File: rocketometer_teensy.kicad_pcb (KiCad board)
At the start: 2 copper layers, 17.8 x 61 mm, 3 parts, among them J101 Teensy4.1, J102 STANDOFF, J103 STANDOFF

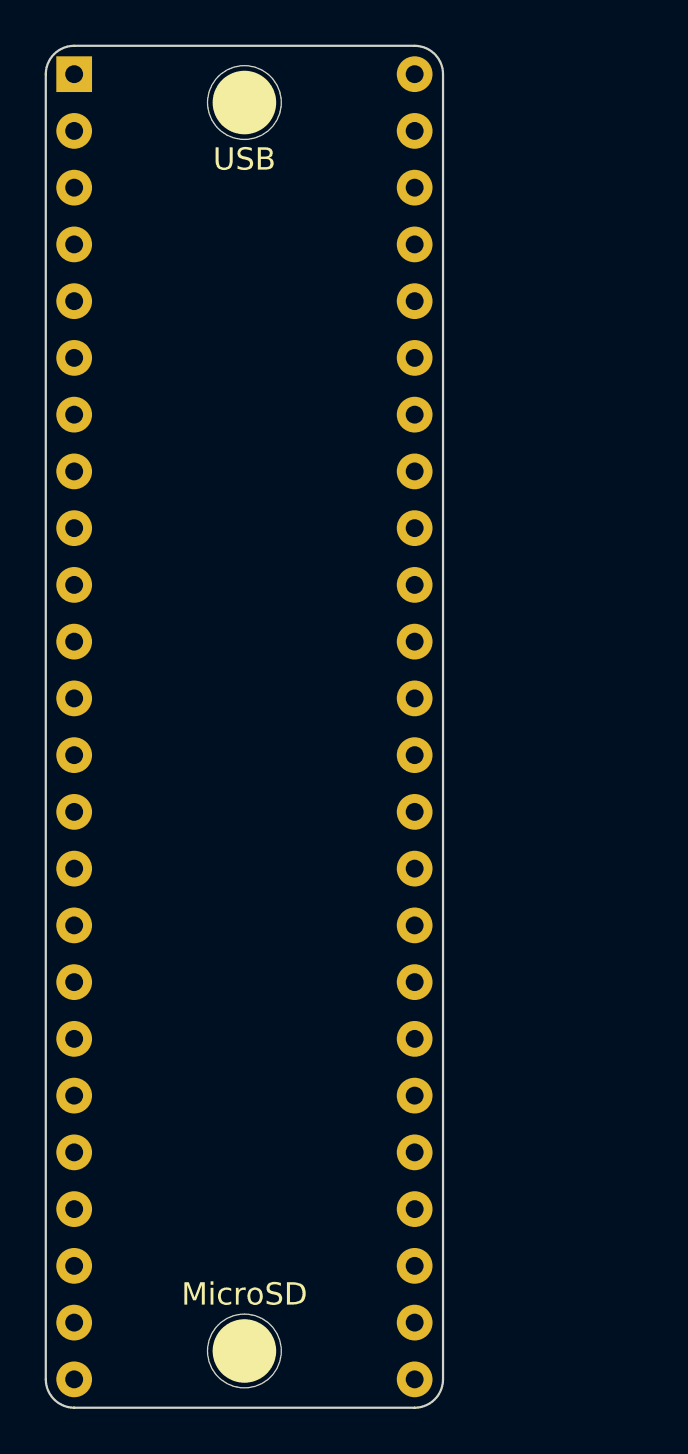
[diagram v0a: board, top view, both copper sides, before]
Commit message: Moved ICM-20948 schematic to kwan_kicad_lib
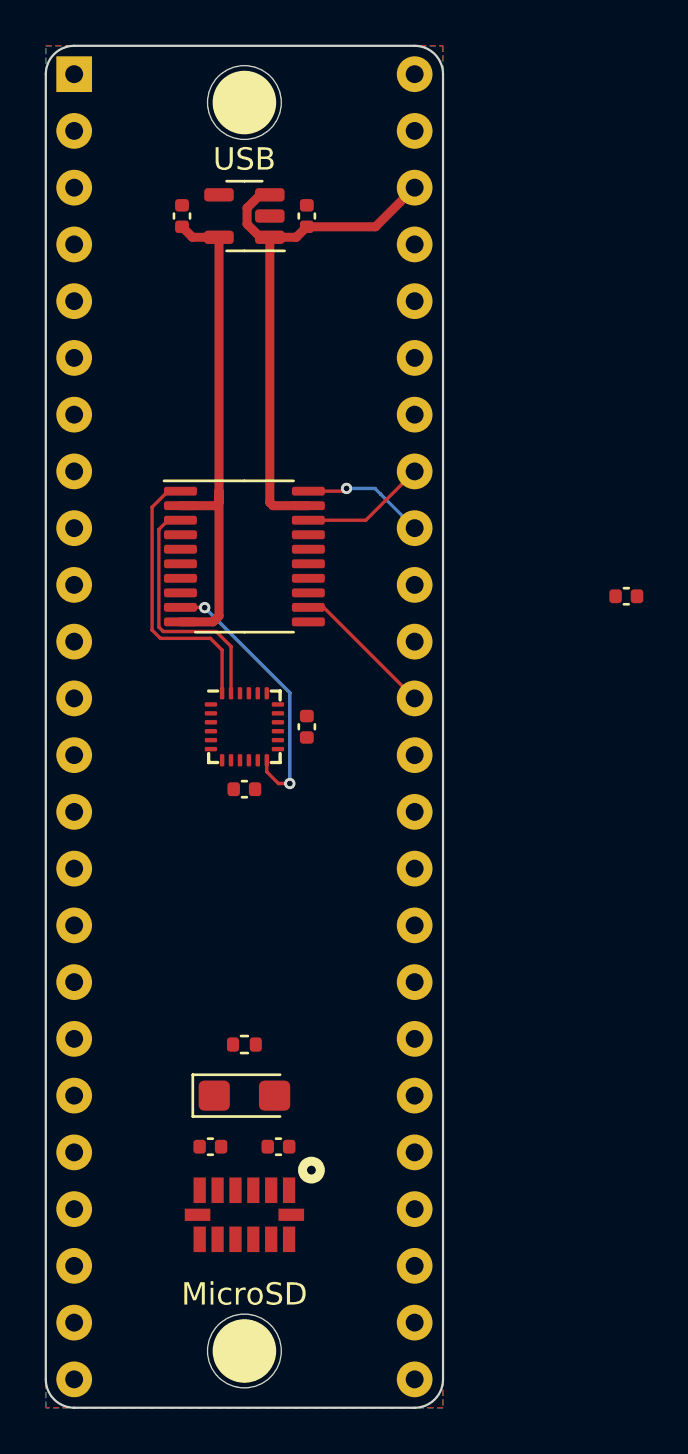
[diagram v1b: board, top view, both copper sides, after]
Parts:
- added C208: 100nF, Capacitor_SMD:C_0402_1005Metric, F.Cu at (138.4, 109.5)
- added C210: 100nF, Capacitor_SMD:C_0402_1005Metric, F.Cu at (155.5, 100.8)
- added C213: 100nF, Capacitor_SMD:C_0402_1005Metric, F.Cu at (141.2, 106.7)
- added C301: 1uF, Capacitor_SMD:C_0402_1005Metric, F.Cu at (141.2, 83.8)
- added C305: 1uF, Capacitor_SMD:C_0402_1005Metric, F.Cu at (135.6, 83.8)
- added C401: 100nF, Capacitor_SMD:C_0402_1005Metric, F.Cu at (140.0, 125.5)
- added C405: 100nF, Capacitor_SMD:C_0402_1005Metric, F.Cu at (136.9, 125.5)
- added C406: 10uF, Capacitor_Tantalum_SMD:CP_EIA-3216-18_Kemet-A, F.Cu at (138.4, 123.2)
- added R406: 100, Resistor_SMD:R_0402_1005Metric, F.Cu at (138.4, 120.9)
- added U101: TXS0108EPW, Package_SO:TSSOP-20_4.4x6.5mm_P0.65mm, F.Cu at (138.4, 99.1)
- added U201: ICM-20948, Sensor_Motion:InvenSense_QFN-24_3x3mm_P0.4mm, F.Cu at (138.4, 106.7)
- added U301: TCR2EF 1.8V, Package_TO_SOT_SMD:SOT-23-5, F.Cu at (138.4, 83.8)
- added U401: ADXL375, KwanSystems:ADXL375, F.Cu at (138.4, 128.5)
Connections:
- J101 pad 1: unconnected-(J101-Pad1) -> GND
- J101 pad 15: unconnected-(J101-Pad15) -> +3V3
- J101 pad 34: unconnected-(J101-Pad34) -> GND
- J101 pad 37: unconnected-(J101-Pad37) -> /IMU_DRDY_3V3
- J101 pad 40: unconnected-(J101-Pad40) -> /SDA_3V3
- J101 pad 41: unconnected-(J101-Pad41) -> /SCL_3V3
- J101 pad 46: unconnected-(J101-Pad46) -> +3V3
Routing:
- net +3V3: track 0.00 -> 24.3 mm
- net +1V8: track 0.00 -> 22.9 mm
- net /SDA_1V8: track 0.00 -> 12.5 mm
- net /IMU_DRDY_1V8: track 0.00 -> 12.3 mm, vias 0 -> 2
- net /SCL_1V8: track 0.00 -> 11.2 mm
- net /IMU_DRDY_3V3: track 0.00 -> 6.45 mm
- net /SCL_3V3: track 0.00 -> 5.66 mm
- net /SDA_3V3: track 0.00 -> 5.54 mm, vias 0 -> 1
- added copper zone on B.Cu, net GND
- added copper zone on F.Cu, net GND
